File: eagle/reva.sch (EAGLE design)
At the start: 233 parts, among them IC1 LM555D, IC2 74HC174D, J1 TYPE-C-31-M-12, U1 TPS63002DRCR

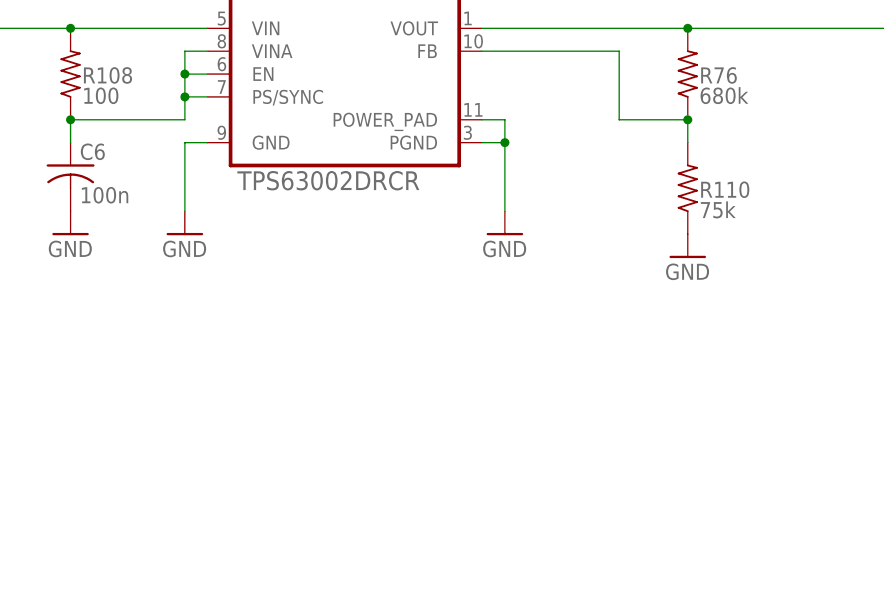
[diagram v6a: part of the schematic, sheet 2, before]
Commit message: Change pads to 0603 and move some resistors around. This commit marks final draft
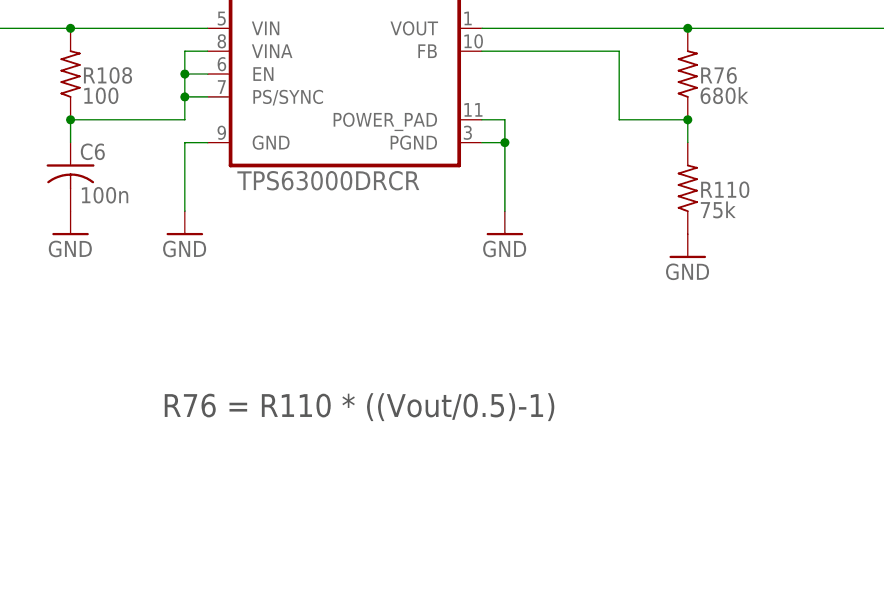
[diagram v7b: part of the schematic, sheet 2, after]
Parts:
- R1, R10, R100, R101, R102, R103, R104, R105, R106, R107, R108, R109, R11, R110, R12, R13, R14, R15, R16, R17, R18, R19, R2, R20, R21, R22, R23, R24, R25, R26, R27, R28, R29, R3, R30, R31, R32, R33, R34, R35, R36, R37, R38, R39, R4, R40, R41, R42, R43, R44, R45, R46, R47, R48, R49, R5, R50, R51, R52, R53, R54, R55, R56, R57, R58, R59, R6, R60, R61, R62, R63, R64, R65, R66, R67, R68, R69, R7, R70, R71, R72, R73, R74, R75, R76, R77, R78, R79, R8, R80, R81, R82, R83, R84, R85, R86, R87, R88, R89, R9, R90, R91, R92, R93, R94, R95, R96, R97, R98, R99: device adafruit:R-US_R0402 -> adafruit:R-US_R0603
- U1: value TPS63002DRCR -> TPS63000DRCR
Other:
- note added: "R76 = R110 * ((Vout/0.5)-1)"

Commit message: Save
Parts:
- R76: value 680k -> 71k
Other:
- note added: "R76 680k for 5V 71k for 2.68V"
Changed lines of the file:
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@@
 <part name="H4" library="holes" library_urn="urn:adsk.eagle:library:237" deviceset="MOUNT-HOLE" device="3.3" package3d_urn="urn:adsk.eagle:package:14278/1"/>
 <part name="BAT1" library="flashing_ece_2025" deviceset="CR2450" device=""/>
-<part name="R76" library="adafruit" deviceset="R-US_" device="R0603" value="680k"/>
+<part name="R76" library="adafruit" deviceset="R-US_" device="R0603" value="71k"/>
 <part name="R110" library="adafruit" deviceset="R-US_" device="R0603" value="75k"/>
 <part name="GND24" library="supply1" library_urn="urn:adsk.eagle:library:371" deviceset="GND" device=""/>
@@
 <text x="302.26" y="10.16" size="6.4516" layer="94">PWR</text>
 <text x="215.9" y="93.98" size="2.54" layer="97">R76 = R110 * ((Vout/0.5)-1)</text>
+<text x="274.32" y="147.32" size="2.54" layer="97">R76
+680k for 5V
+71k for 2.68V</text>
 </plain>
 <instances>
@@
 </drawing>
 <compatibility>
+<note version="6.3" minversion="6.2.2" severity="warning">
+Since Version 6.2.2 text objects can contain more than one line,
+which will not be processed correctly with this version.
+</note>
 <note version="8.2" severity="warning">
 Since Version 8.2, EAGLE supports online libraries. The ids
